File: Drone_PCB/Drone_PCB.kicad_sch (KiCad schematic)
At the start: 59 parts, among them J1 Conn_01x04_Pin, J2 Conn_01x08_Socket, J3 Conn_01x05_Socket, J4 Conn_01x02_Socket, J5 Conn_01x02_Socket, J6 Conn_01x02_Socket, J7 Conn_01x02_Socket, J8 Conn_01x02_Socket, J9 USB_B_Micro, Q1 AO3400A, Q2 AO3400A, Q3 AO3400A, Q4 AO3400A, Q5 AO3400A, Q6 AO3400A, SW1 SW_Push, SW2 SW_SPST, U1 STM32F411RCT6, U2 AP2112K-3.3, U3 TP4056-42-ESOP8, U4 DW01A, Y1 26MHz

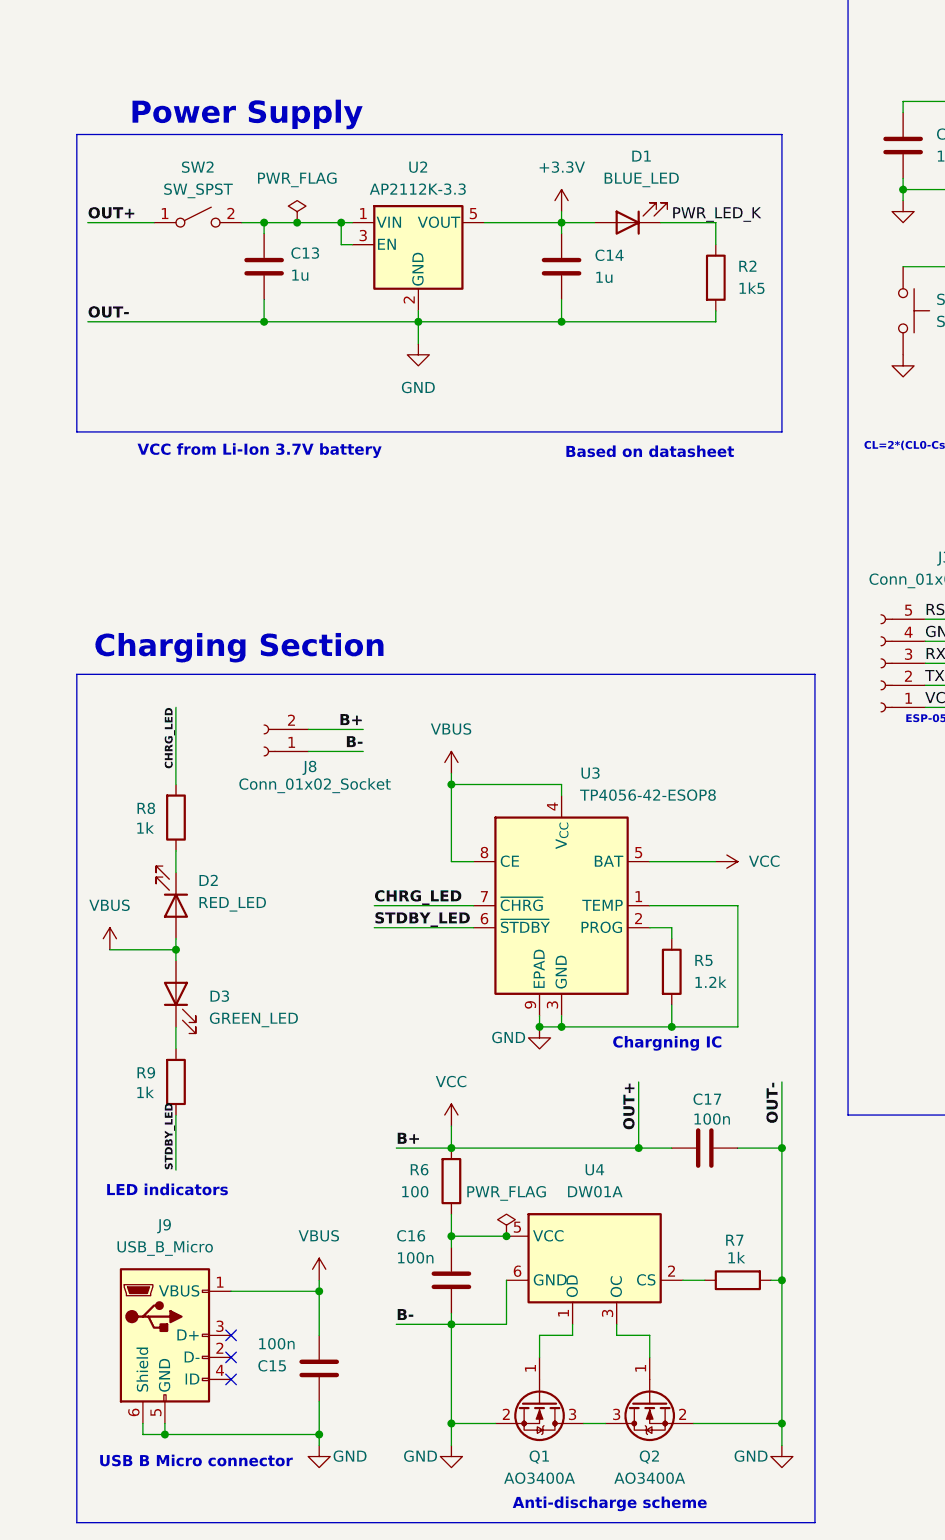
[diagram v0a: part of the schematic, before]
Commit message: PCB #2
Created charging section
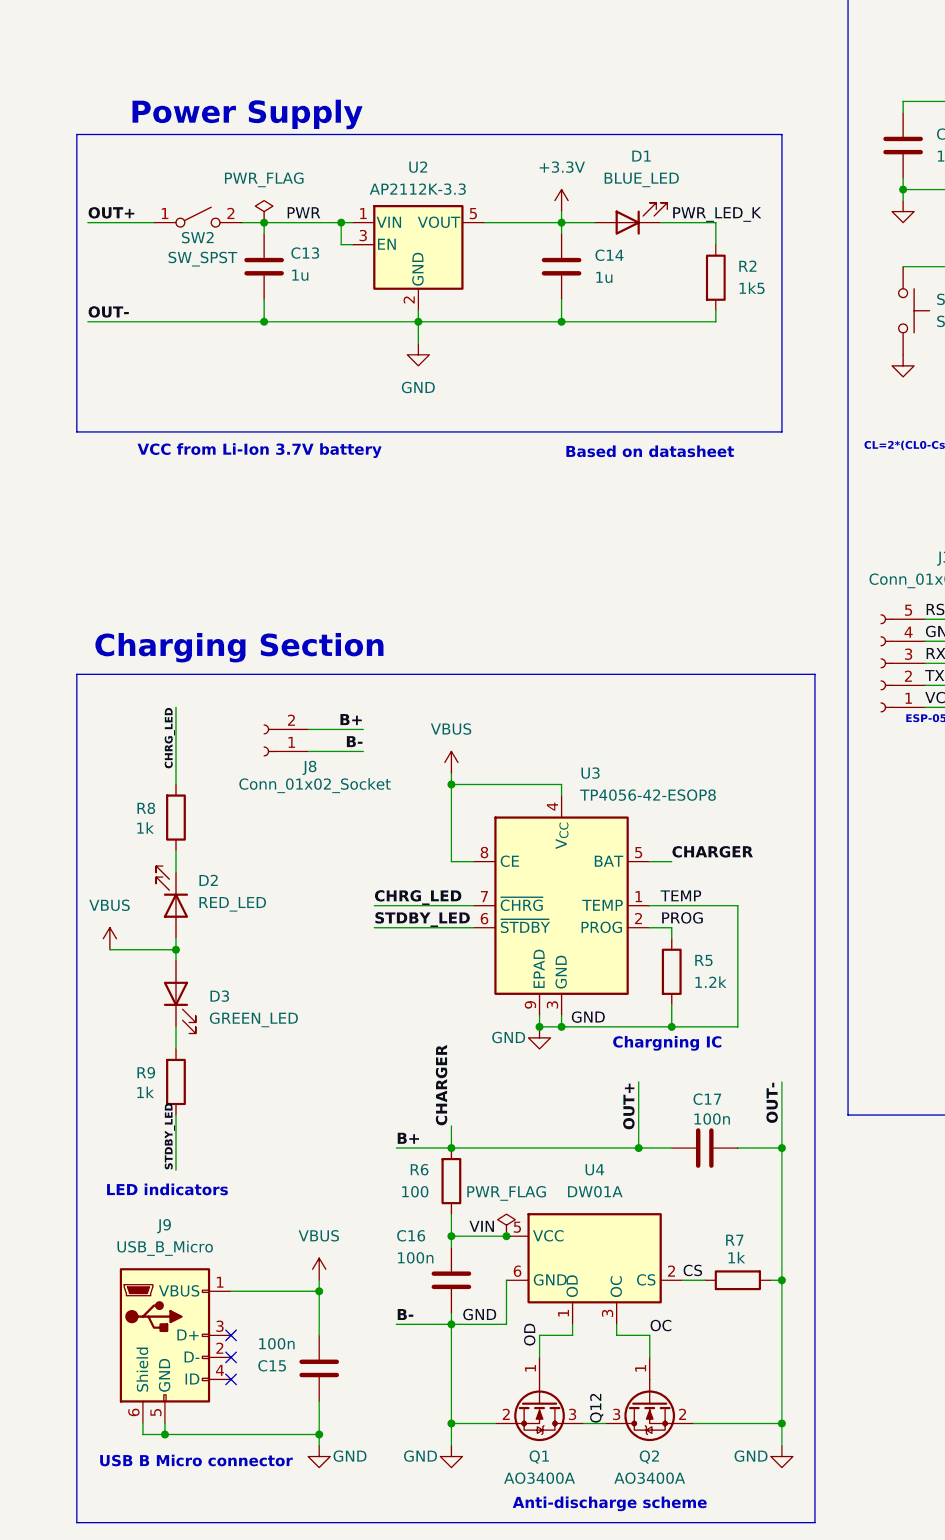
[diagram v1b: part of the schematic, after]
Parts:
- SW2: footprint Button_Switch_SMD:SW_DIP_SPSTx01_Slide_6.7x4.1mm_W6.73mm_P2.54mm_LowProfile_JPin -> Button_Switch_THT:SW_CK_JS202011AQN_DPDT_Angled
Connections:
- net +3.3V: no longer C17.1, J8.2 (Pin_2), R6.2, SW2.1 (A), U3.5 (BAT)
- net VIN: now reaches C16.1, R6.1, U4.5 (VCC)
- net PWR: now reaches C13.1, SW2.2 (B), U2.1 (VIN), U2.3 (EN)
- net OD: now reaches Q1.1 (G), U4.1 (OD)
- net Q12: now reaches Q1.3 (D), Q2.3 (D)
- net CS: now reaches R7.1, U4.2 (CS)
- net OC: now reaches Q2.1 (G), U4.3 (OC)
- net PROG: now reaches R5.1, U3.2 (PROG)
- new net B+: C17.1, J8.2 (Pin_2), R6.2, SW2.1 (A), U3.5 (BAT)
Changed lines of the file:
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@@
 		(color 0 0 0 0)
 	)
-	(junction
-		(at 43.18 45.72)
-		(diameter 0)
-		(color 0 0 0 0)
-	)
 	(no_connect
 		(at 167.64 101.6)
@@
 	(wire
 		(pts
+			(xy 83.82 119.38) (xy 86.36 119.38)
+		)
+		(stroke
+			(width 0)
+			(type default)
+		)
+	)
+	(wire
+		(pts
 			(xy 120.65 105.41) (xy 120.65 93.98)
 		)
@@
 	(wire
 		(pts
-			(xy 83.82 119.38) (xy 91.44 119.38)
-		)
-		(stroke
-			(width 0)
-			(type default)
-		)
-	)
-	(wire
-		(pts
 			(xy 73.66 46.99) (xy 73.66 45.72)
 		)
@@
 	(wire
 		(pts
-			(xy 43.18 45.72) (xy 48.26 45.72)
-		)
-		(stroke
-			(width 0)
-			(type default)
-		)
-	)
-	(wire
-		(pts
 			(xy 203.2 109.22) (xy 205.74 109.22)
 		)
@@
 	(wire
 		(pts
-			(xy 39.37 45.72) (xy 43.18 45.72)
+			(xy 39.37 45.72) (xy 48.26 45.72)
 		)
 		(stroke
@@
 		)
 	)
+	(label "PWR"
+		(at 41.91 45.72 0)
+		(effects
+			(font
+				(size 1.27 1.27)
+			)
+			(justify left bottom)
+		)
+	)
 	(label "GND"
 		(at 115.57 93.98 0)
@@
 		)
 	)
+	(label "TEMP"
+		(at 85.09 124.46 0)
+		(effects
+			(font
+				(size 1.27 1.27)
+			)
+			(justify left bottom)
+		)
+	)
 	(label "OUT+"
 		(at 82.55 144.78 270)
@@
 		)
 	)
+	(label "GND"
+		(at 78.74 138.43 180)
+		(effects
+			(font
+				(size 1.27 1.27)
+			)
+			(justify right bottom)
+		)
+	)
 	(label "HSE_IN"
 		(at 158.75 60.96 0)
@@
 		)
 	)
+	(label "CS"
+		(at 87.63 167.64 0)
+		(effects
+			(font
+				(size 1.27 1.27)
+			)
+			(justify left bottom)
+		)
+	)
 	(label "NRST"
 		(at 157.48 50.8 0)
@@
 		)
 	)
+	(label "GND"
+		(at 62.23 172.72 0)
+		(effects
+			(font
+				(size 1.27 1.27)
+			)
+			(justify left bottom)
+		)
+	)
 	(label "MOTOR_LF"
 		(at 204.47 73.66 0)
@@
 		)
 	)
+	(label "Q12"
+		(at 78.74 184.15 90)
+		(effects
+			(font
+				(size 1.27 1.27)
+			)
+			(justify left bottom)
+		)
+	)
 	(label "ADO"
 		(at 237.49 124.46 180)
@@
 		)
 	)
+	(label "OD"
+		(at 71.12 175.26 90)
+		(effects
+			(font
+				(size 1.27 1.27)
+			)
+			(justify left bottom)
+		)
+	)
+	(label "OC"
+		(at 83.82 173.99 0)
+		(effects
+			(font
+				(size 1.27 1.27)
+			)
+			(justify left bottom)
+		)
+	)
 	(label "SWCLK"
 		(at 220.98 110.49 0)
@@
 		)
 	)
+	(label "VIN"
+		(at 66.04 162.56 180)
+		(effects
+			(font
+				(size 1.27 1.27)
+			)
+			(justify right bottom)
+		)
+	)
+	(label "CHARGER"
+		(at 60.96 149.86 90)
+		(effects
+			(font
+				(size 1.27 1.27)
+				(thickness 0.254)
+				(bold yes)
+			)
+			(justify left bottom)
+		)
+	)
 	(label "LED_SIGNAL"
 		(at 156.21 96.52 0)
@@
 		)
 	)
+	(label "CHARGER"
+		(at 86.36 119.38 0)
+		(effects
+			(font
+				(size 1.27 1.27)
+				(thickness 0.254)
+				(bold yes)
+			)
+			(justify left bottom)
+		)
+	)
 	(label "SCL"
 		(at 237.49 134.62 180)
@@
 		)
 	)
+	(label "PROG"
+		(at 85.09 127 0)
+		(effects
+			(font
+				(size 1.27 1.27)
+			)
+			(justify left bottom)
+		)
+	)
 	(label "TX"
 		(at 115.57 99.06 0)
@@
 		(on_board yes)
 		(dnp no)
-		(fields_autoplaced yes)
 		(property "Reference" "SW2"
-			(at 31.75 39.37 0)
+			(at 31.75 47.498 0)
 			(effects
 				(font
@@
 		)
 		(property "Value" "SW_SPST"
-			(at 31.75 41.91 0)
+			(at 32.258 49.784 0)
 			(effects
 				(font
@@
 			)
 		)
-		(property "Footprint" "Button_Switch_SMD:SW_DIP_SPSTx01_Slide_6.7x4.1mm_W6.73mm_P2.54mm_LowProfile_JPin"
+		(property "Footprint" "Button_Switch_THT:SW_CK_JS202011AQN_DPDT_Angled"
 			(at 31.75 45.72 0)
 			(effects
@@
 	)
 	(symbol
-		(lib_id "power:VCC")
-		(at 91.44 119.38 270)
-		(unit 1)
-		(exclude_from_sim no)
-		(in_bom yes)
-		(on_board yes)
-		(dnp no)
-		(fields_autoplaced yes)
-		(property "Reference" "#PWR030"
-			(at 87.63 119.38 0)
-			(effects
-				(font
-					(size 1.27 1.27)
-				)
-				(hide yes)
-			)
-		)
-		(property "Value" "VCC"
-			(at 95.25 119.3799 90)
-			(effects
-				(font
-					(size 1.27 1.27)
-				)
-				(justify left)
-			)
-		)
-		(property "Footprint" ""
-			(at 91.44 119.38 0)
-			(effects
-				(font
-					(size 1.27 1.27)
-				)
-				(hide yes)
-			)
-		)
-		(property "Datasheet" ""
-			(at 91.44 119.38 0)
-			(effects
-				(font
-					(size 1.27 1.27)
-				)
-				(hide yes)
-			)
-		)
-		(property "Description" "Power symbol creates a global label with name \"VCC\""
-			(at 91.44 119.38 0)
-			(effects
-				(font
-					(size 1.27 1.27)
-				)
-				(hide yes)
-			)
-		)
-		(pin "1"
-		)
-		(instances
-			(project ""
-				(path "/2c198202-91eb-4035-8605-360d42f3c3f5"
-					(reference "#PWR030")
-					(unit 1)
-				)
-			)
-		)
-	)
-	(symbol
 		(lib_name "AO3400A_2")
 		(lib_id "Transistor_FET:AO3400A")
@@
 	(symbol
 		(lib_id "power:PWR_FLAG")
-		(at 43.18 45.72 0)
+		(at 39.37 45.72 0)
 		(unit 1)
 		(exclude_from_sim no)
@@
 		(fields_autoplaced yes)
 		(property "Reference" "#FLG03"
-			(at 43.18 43.815 0)
+			(at 39.37 43.815 0)
 			(effects
 				(font
@@
 		)
 		(property "Value" "PWR_FLAG"
-			(at 43.18 40.64 0)
+			(at 39.37 40.64 0)
 			(effects
 				(font
@@
 		)
 		(property "Footprint" ""
-			(at 43.18 45.72 0)
+			(at 39.37 45.72 0)
 			(effects
 				(font
@@
 		)
 		(property "Datasheet" "~"
-			(at 43.18 45.72 0)
+			(at 39.37 45.72 0)
 			(effects
 				(font
@@
 		)
 		(property "Description" "Special symbol for telling ERC where power comes from"
-			(at 43.18 45.72 0)
+			(at 39.37 45.72 0)
 			(effects
 				(font
@@
 					(unit 1)
 				)
-			)
-		)
-	)
-	(symbol
-		(lib_id "power:VCC")
-		(at 60.96 149.86 0)
-		(unit 1)
-		(exclude_from_sim no)
-		(in_bom yes)
-		(on_board yes)
-		(dnp no)
-		(fields_autoplaced yes)
-		(property "Reference" "#PWR031"
-			(at 60.96 153.67 0)
-			(effects
-				(font
-					(size 1.27 1.27)
-				)
-				(hide yes)
-			)
-		)
-		(property "Value" "VCC"
-			(at 60.96 144.78 0)
-			(effects
-				(font
-					(size 1.27 1.27)
-				)
-			)
-		)
-		(property "Footprint" ""
-			(at 60.96 149.86 0)
-			(effects
-				(font
-					(size 1.27 1.27)
-				)
-				(hide yes)
-			)
-		)
-		(property "Datasheet" ""
-			(at 60.96 149.86 0)
-			(effects
-				(font
-					(size 1.27 1.27)
-				)
-				(hide yes)
-			)
-		)
-		(property "Description" "Power symbol creates a global label with name \"VCC\""
-			(at 60.96 149.86 0)
-			(effects
-				(font
-					(size 1.27 1.27)
-				)
-				(hide yes)
-			)
-		)
-		(pin "1"
-		)
-		(instances
-			(project "Drone_PCB"
-				(path "/2c198202-91eb-4035-8605-360d42f3c3f5"
-					(reference "#PWR031")
-					(unit 1)
-				)

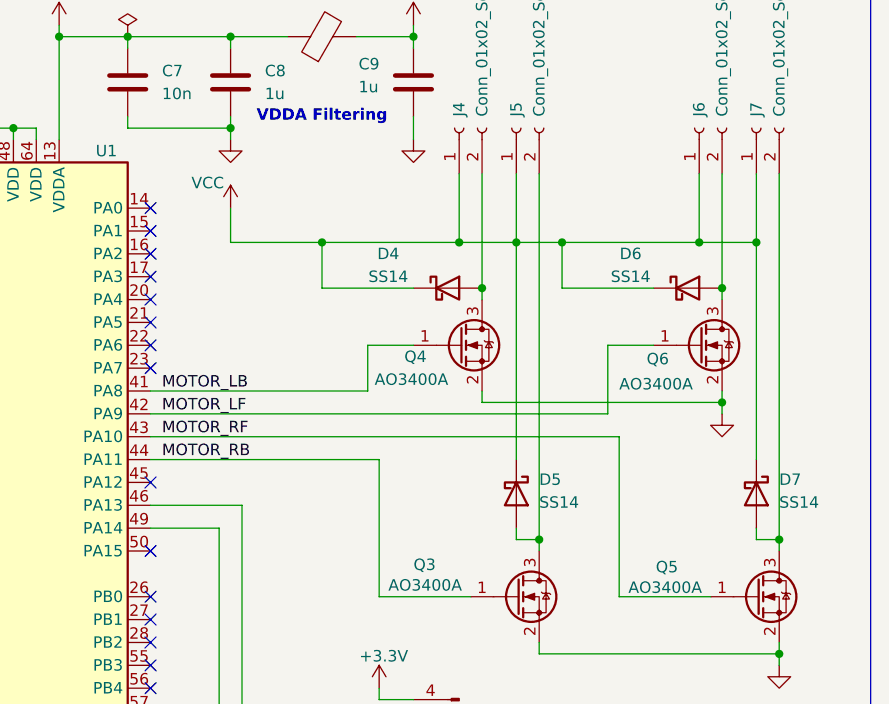
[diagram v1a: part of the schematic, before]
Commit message: PCB #3
Added motors
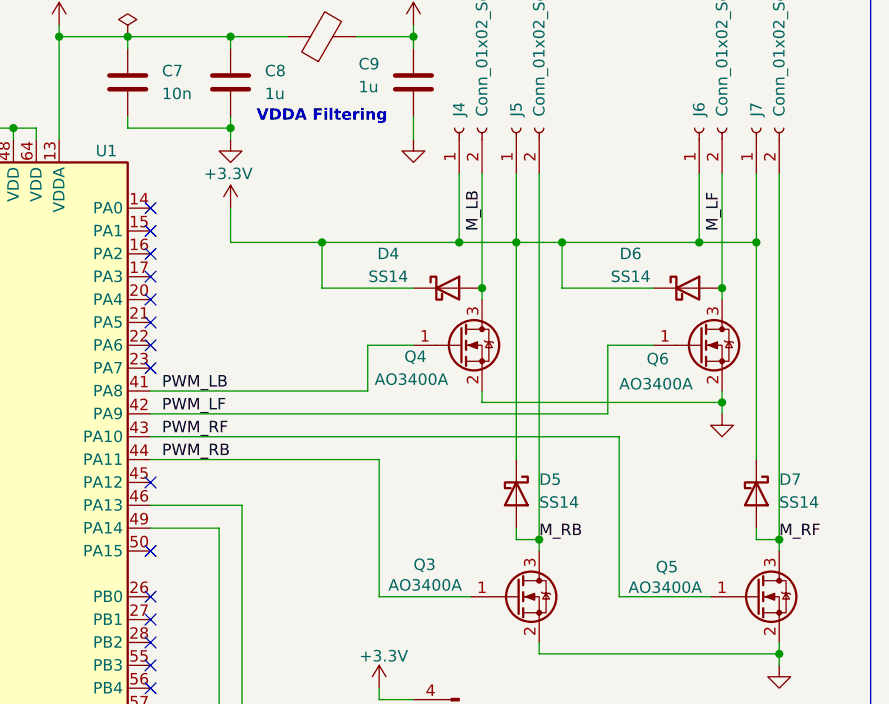
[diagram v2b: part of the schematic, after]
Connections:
- net M_LB: now reaches D4.2 (A), J4.2 (Pin_2), Q4.3 (D)
- net M_RF: now reaches D7.2 (A), J7.2 (Pin_2), Q5.3 (D)
- net M_LF: now reaches D6.2 (A), J6.2 (Pin_2), Q6.3 (D)
- net M_RB: now reaches D5.2 (A), J5.2 (Pin_2), Q3.3 (D)
- net MOTOR_LB renamed PWM_LB
- net MOTOR_LF renamed PWM_LF
- net MOTOR_RB renamed PWM_RB
- net MOTOR_RF renamed PWM_RF
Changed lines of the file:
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@@
 		)
 	)
+	(label "M_RB"
+		(at 246.38 87.63 0)
+		(effects
+			(font
+				(size 1.27 1.27)
+			)
+			(justify left bottom)
+		)
+	)
 	(label "TEMP"
 		(at 85.09 124.46 0)
@@
 		)
 	)
+	(label "M_LF"
+		(at 266.7 53.34 90)
+		(effects
+			(font
+				(size 1.27 1.27)
+			)
+			(justify left bottom)
+		)
+	)
 	(label "OUT+"
 		(at 19.05 45.72 0)
@@
 		)
 	)
-	(label "MOTOR_RF"
+	(label "PWM_RF"
 		(at 204.47 76.2 0)
 		(effects
@@
 		)
 	)
-	(label "MOTOR_LB"
+	(label "PWM_LB"
 		(at 204.47 71.12 0)
 		(effects
@@
 		)
 	)
-	(label "MOTOR_LF"
+	(label "PWM_LF"
 		(at 204.47 73.66 0)
 		(effects
@@
 		)
 	)
-	(label "MOTOR_RB"
+	(label "PWM_RB"
 		(at 204.47 78.74 0)
 		(effects
@@
 		)
 	)
+	(label "M_RF"
+		(at 273.05 87.63 0)
+		(effects
+			(font
+				(size 1.27 1.27)
+			)
+			(justify left bottom)
+		)
+	)
 	(label "BOOT0"
 		(at 160.02 55.88 0)
@@
 		)
 	)
+	(label "M_LB"
+		(at 240.03 53.34 90)
+		(effects
+			(font
+				(size 1.27 1.27)
+			)
+			(justify left bottom)
+		)
+	)
 	(label "INT"
 		(at 237.49 121.92 180)
@@
 	)
 	(symbol
-		(lib_id "power:VCC")
-		(at 212.09 50.8 0)
-		(unit 1)
-		(exclude_from_sim no)
-		(in_bom yes)
-		(on_board yes)
-		(dnp no)
-		(property "Reference" "#PWR022"
-			(at 212.09 54.61 0)
-			(effects
-				(font
-					(size 1.27 1.27)
-				)
-				(hide yes)
-			)
-		)
-		(property "Value" "VCC"
-			(at 209.55 48.006 0)
-			(effects
-				(font
-					(size 1.27 1.27)
-				)
-			)
-		)
-		(property "Footprint" ""
-			(at 212.09 50.8 0)
-			(effects
-				(font
-					(size 1.27 1.27)
-				)
-				(hide yes)
-			)
-		)
-		(property "Datasheet" ""
-			(at 212.09 50.8 0)
-			(effects
-				(font
-					(size 1.27 1.27)
-				)
-				(hide yes)
-			)
-		)
-		(property "Description" "Power symbol creates a global label with name \"VCC\""
-			(at 212.09 50.8 0)
-			(effects
-				(font
-					(size 1.27 1.27)
-				)
-				(hide yes)
-			)
-		)
-		(pin "1"
-		)
-		(instances
-			(project "Drone_PCB"
-				(path "/2c198202-91eb-4035-8605-360d42f3c3f5"
-					(reference "#PWR022")
-					(unit 1)
-				)
-			)
-		)
-	)
-	(symbol
 		(lib_id "power:GND")
 		(at 113.03 60.96 0)
@@
 					(unit 1)
 				)
+			)
+		)
+	)
+	(symbol
+		(lib_id "power:+3.3V")
+		(at 212.09 50.8 0)
+		(unit 1)
+		(exclude_from_sim no)
+		(in_bom yes)
+		(on_board yes)
+		(dnp no)
+		(property "Reference" "#PWR022"
+			(at 212.09 54.61 0)
+			(effects
+				(font
+					(size 1.27 1.27)
+				)
+				(hide yes)
+			)
+		)
+		(property "Value" "+3.3V"
+			(at 211.836 46.99 0)
+			(effects
+				(font
+					(size 1.27 1.27)
+				)
+			)
+		)
+		(property "Footprint" ""
+			(at 212.09 50.8 0)
+			(effects
+				(font
+					(size 1.27 1.27)
+				)
+				(hide yes)
+			)
+		)
+		(property "Datasheet" ""
+			(at 212.09 50.8 0)
+			(effects
+				(font
+					(size 1.27 1.27)
+				)
+				(hide yes)
+			)
+		)
+		(property "Description" "Power symbol creates a global label with name \"+3.3V\""
+			(at 212.09 50.8 0)
+			(effects
+				(font
+					(size 1.27 1.27)
+				)
+				(hide yes)
+			)
+		)
+		(pin "1"
+		)
+		(instances
+			(project "Drone_PCB"
+				(path "/2c198202-91eb-4035-8605-360d42f3c3f5"
+					(reference "#PWR022")
+					(unit 1)
+				)

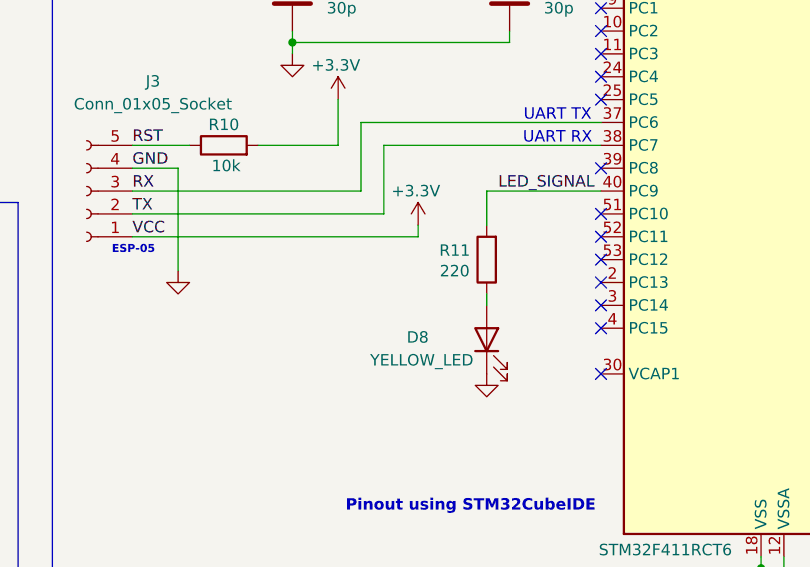
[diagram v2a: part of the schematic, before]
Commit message: PCB #4
Connected signal LED, everything is connected
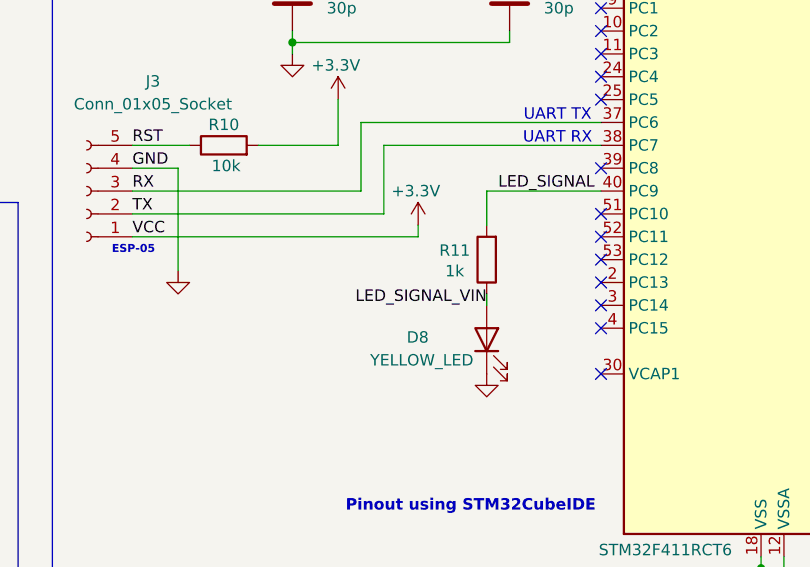
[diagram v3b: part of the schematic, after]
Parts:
- R11: value 220 -> 1k
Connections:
- net LED_SIGNAL_VIN: now reaches D8.2 (A), R11.1
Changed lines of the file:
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@@
 		)
 	)
+	(label "LED_SIGNAL_VIN"
+		(at 154.94 109.22 180)
+		(effects
+			(font
+				(size 1.27 1.27)
+			)
+			(justify right bottom)
+		)
+	)
 	(label "HSE_OUT"
 		(at 158.75 63.5 0)
@@
 			)
 		)
-		(property "Value" "220"
+		(property "Value" "1k"
 			(at 151.384 105.41 0)
 			(effects
